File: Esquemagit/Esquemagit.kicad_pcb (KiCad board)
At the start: 2 copper layers, 25 parts, among them U1 LM358, U5 ESP32-WROOM-32

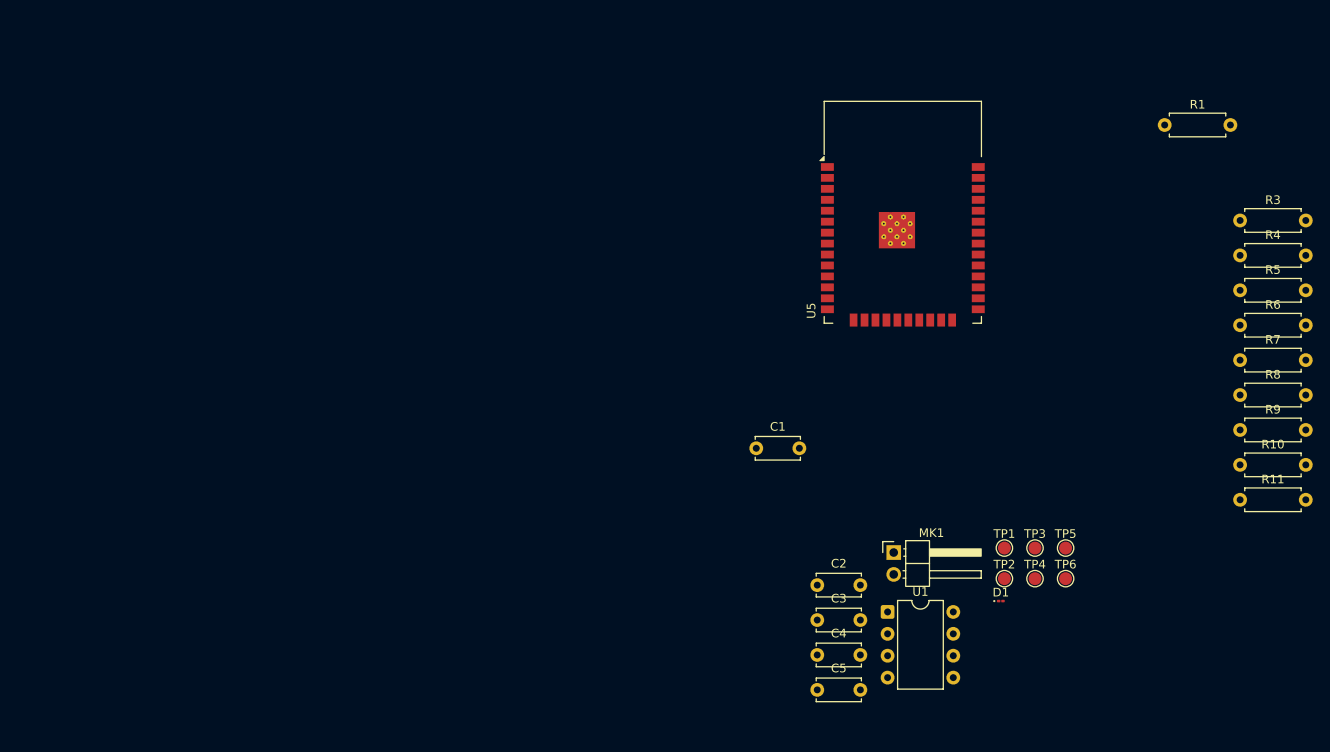
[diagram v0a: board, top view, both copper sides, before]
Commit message: Se agrego huellas, se realizo avances en la etapa de amplificacion en la pcb
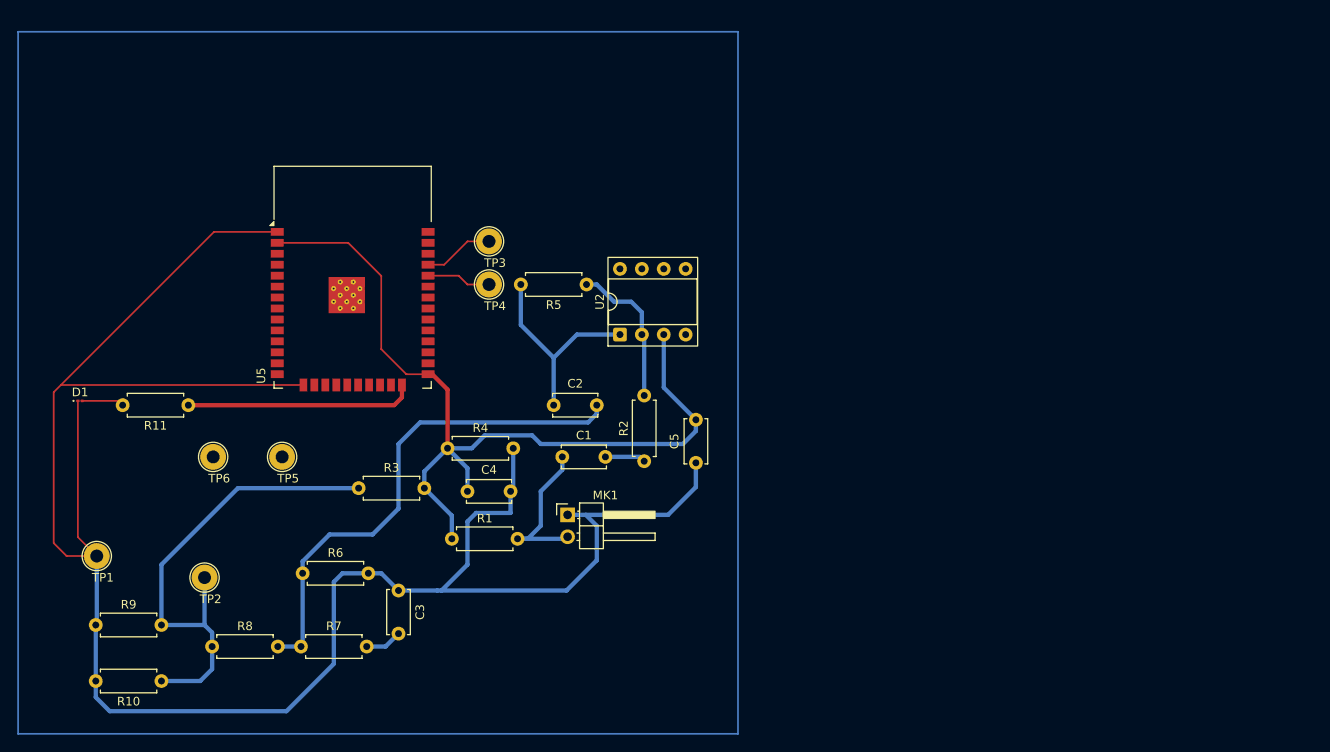
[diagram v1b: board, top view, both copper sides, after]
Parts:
- removed U1: LM358, Package_DIP:DIP-8_W7.62mm
- added R2: 1K, Resistor_THT:R_Axial_DIN0207_L6.3mm_D2.5mm_P7.62mm_Horizontal, F.Cu at (99.5, 103.0)
- added U2: LM358, Package_DIP:DIP-8_W7.62mm_Socket, F.Cu at (96.7, 88.3)
- TP1, TP2, TP3, TP4, TP5, TP6: footprint TestPoint:TestPoint_Pad_D1.5mm -> TestPoint:TestPoint_Loop_D2.54mm_Drill1.5mm_Beaded
- moved R9 134.7 mm to (35.9, 122.0)
- moved R10 127.6 mm to (43.5, 128.5), turned to 180 degrees
- moved R8 122.8 mm to (49.4, 124.5)
- moved R11 122.5 mm to (46.6, 96.5), turned to 180 degrees
- moved R7 113.9 mm to (59.7, 124.5)
- moved R6 112.5 mm to (59.9, 116.0)
- moved D1 109.3 mm to (34.1, 96.0)
- moved R3 106.9 mm to (66.4, 106.1)
- moved TP1 105.3 mm to (36.0, 114.0)
- moved TP6 99.9 mm to (49.5, 102.5)
- moved R1 95.6 mm to (77.2, 112.0)
- moved R4 94.6 mm to (76.7, 101.5)
- moved TP2 92.8 mm to (48.5, 116.5)
- moved TP5 91.5 mm to (57.5, 102.5)
- moved R5 75.8 mm to (92.8, 82.5), turned to 180 degrees
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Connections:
- TP2 pad 1: /+3.3V -> 3.3V
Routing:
- net GND: track 0.00 -> 247.3 mm
- net 3.3V: track 0.00 -> 156.7 mm
- net Net-(C2-Pad2): track 0.00 -> 59.3 mm
- net /LED_CTRL: track 0.00 -> 26.6 mm
- net Net-(C2-Pad1): track 0.00 -> 24.4 mm
- net Net-(MK1-+): track 0.00 -> 18.2 mm
- net Net-(U2A--): track 0.00 -> 17.5 mm
- net /TX: track 0.00 -> 8.19 mm
- net /RX: track 0.00 -> 7.49 mm
- net Net-(D1-A): track 0.00 -> 4.90 mm
- net Net-(C1-Pad2): track 0.00 -> 4.71 mm
- net Net-(C3-Pad2): track 0.00 -> 4.31 mm

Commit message: Realice ajustes de componenetes en pcb y ademas cableado de pistas
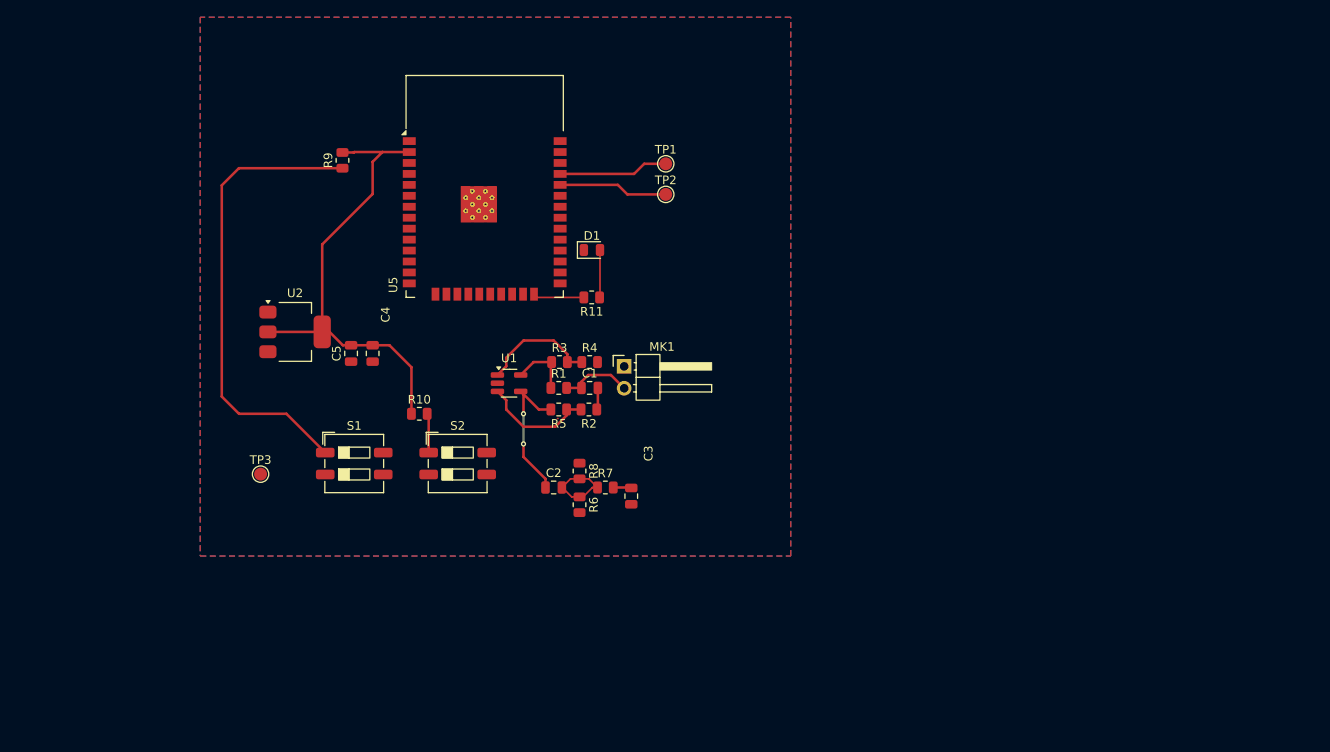
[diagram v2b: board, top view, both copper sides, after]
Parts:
- removed TP4, TP5, TP6: TestPoint, TestPoint:TestPoint_Loop_D2.54mm_Drill1.5mm_Beaded
- added S1: PulsadorMTR_LFS, Button_Switch_SMD:SW_DIP_SPSTx02_Slide_6.7x6.64mm_W6.73mm_P2.54mm_LowProfile_JPin, F.Cu at (65.9, 103.3)
- added S2: PulsadorMTR_LFS, Button_Switch_SMD:SW_DIP_SPSTx02_Slide_6.7x6.64mm_W6.73mm_P2.54mm_LowProfile_JPin, F.Cu at (77.9, 103.3)
- added U1: LMV321, Package_TO_SOT_SMD:SOT-23-5_HandSoldering, F.Cu at (83.8, 94.0)
- C1, C2, C3, C4, C5: footprint Capacitor_THT:C_Disc_D5.0mm_W2.5mm_P5.00mm -> Capacitor_SMD:C_0805_2012Metric
- D1: footprint LED_SMD:LED_01005_0402Metric -> LED_SMD:LED_0805_2012Metric
- R1, R11, R2, R3, R4, R5, R6, R7, R8, R9: footprint Resistor_THT:R_Axial_DIN0207_L6.3mm_D2.5mm_P7.62mm_Horizontal -> Resistor_SMD:R_0805_2012Metric
- R10: value R -> 10; footprint Resistor_THT:R_Axial_DIN0207_L6.3mm_D2.5mm_P7.62mm_Horizontal -> Resistor_SMD:R_0805_2012Metric
- TP1, TP2, TP3: footprint TestPoint:TestPoint_Loop_D2.54mm_Drill1.5mm_Beaded -> TestPoint:TestPoint_Pad_D1.5mm
- U2: value LM358 -> AMS1117-3.3; footprint Package_DIP:DIP-8_W7.62mm_Socket -> Package_TO_SOT_SMD:SOT-223-3_TabPin2
- moved TP1 80.2 mm to (102.0, 68.5)
- moved TP2 69.6 mm to (102.0, 72.0)
- moved D1 61.9 mm to (93.4, 78.5)
- moved R9 61.0 mm to (64.5, 68.1), turned to 90 degrees
- moved R11 48.4 mm to (93.4, 84.0)
- moved R8 47.2 mm to (92.0, 104.1), turned to -90 degrees
- moved R10 43.1 mm to (73.4, 97.5), turned to 0 degrees
- moved C5 42.0 mm to (65.5, 90.5)
- moved R7 39.8 mm to (95.0, 106.0)
- moved TP3 37.8 mm to (55.0, 104.5)
- moved U2 37.7 mm to (59.0, 88.0), turned to 0 degrees
- moved R6 33.1 mm to (92.0, 108.0), turned to -90 degrees
- moved C3 29.1 mm to (98.0, 107.0), turned to 90 degrees
- moved R3 27.5 mm to (89.7, 91.5)
- moved R1 21.4 mm to (89.6, 94.5)
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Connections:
- C2 pad 1: Net-(C2-Pad1) -> /salida
- R10 pad 2: GND -> Net-(S2-COM)
- R11 pad 1: /LED_CTRL -> Net-(D1-A)
- R11 pad 2: Net-(D1-A) -> /LED_CTRL
- R2 pad 2: Net-(U2A--) -> Net-(U1--)
- R3 pad 2: 3.3V -> Net-(U1-+)
- R4 pad 1: 3.3V -> Net-(U1-+)
- R5 pad 1: Net-(U2A--) -> Net-(U1--)
- R5 pad 2: Net-(C2-Pad1) -> /salida
- R9 pad 1: GND -> Net-(S1-COM)
- TP1 pad 1: GND -> /TX
- TP2 pad 1: 3.3V -> /RX
- TP3 pad 1: /TX -> GND
- U2 pad 1: Net-(C2-Pad1) -> Net-(J2-GND_1)
- U2 pad 2: Net-(U2A--) -> 3.3V
- U2 pad 3: 3.3V -> Net-(J2-VBUS_1)
- U5 pad 25: 3.3V -> Net-(S2-COM)
- U5 pad 3: GND -> Net-(S1-COM)
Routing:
- net GND: track 247.3 -> 0.00 mm
- net 3.3V: track 156.7 -> 62.5 mm
- net Net-(S1-COM): track 0.00 -> 54.0 mm
- net Net-(C2-Pad2): track 59.3 -> 10.0 mm
- net Net-(C2-Pad1): track 24.4 -> 0.00 mm
- net /LED_CTRL: track 26.6 -> 5.94 mm
- net Net-(U2A--): track 17.5 -> 0.00 mm
- net /salida: track 0.00 -> 16.7 mm, vias 0 -> 2
- net Net-(U1-+): track 0.00 -> 13.6 mm
- net Net-(U1--): track 0.00 -> 13.3 mm
- net Net-(MK1-+): track 18.2 -> 8.36 mm
- net /RX: track 7.49 -> 12.7 mm
- net Net-(S2-COM): track 0.00 -> 4.57 mm
- net /TX: track 8.19 -> 12.7 mm
- net Net-(C3-Pad2): track 4.31 -> 2.11 mm
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- added copper zone on B.Cu, net GND
- added copper zone on F.Cu, net GND

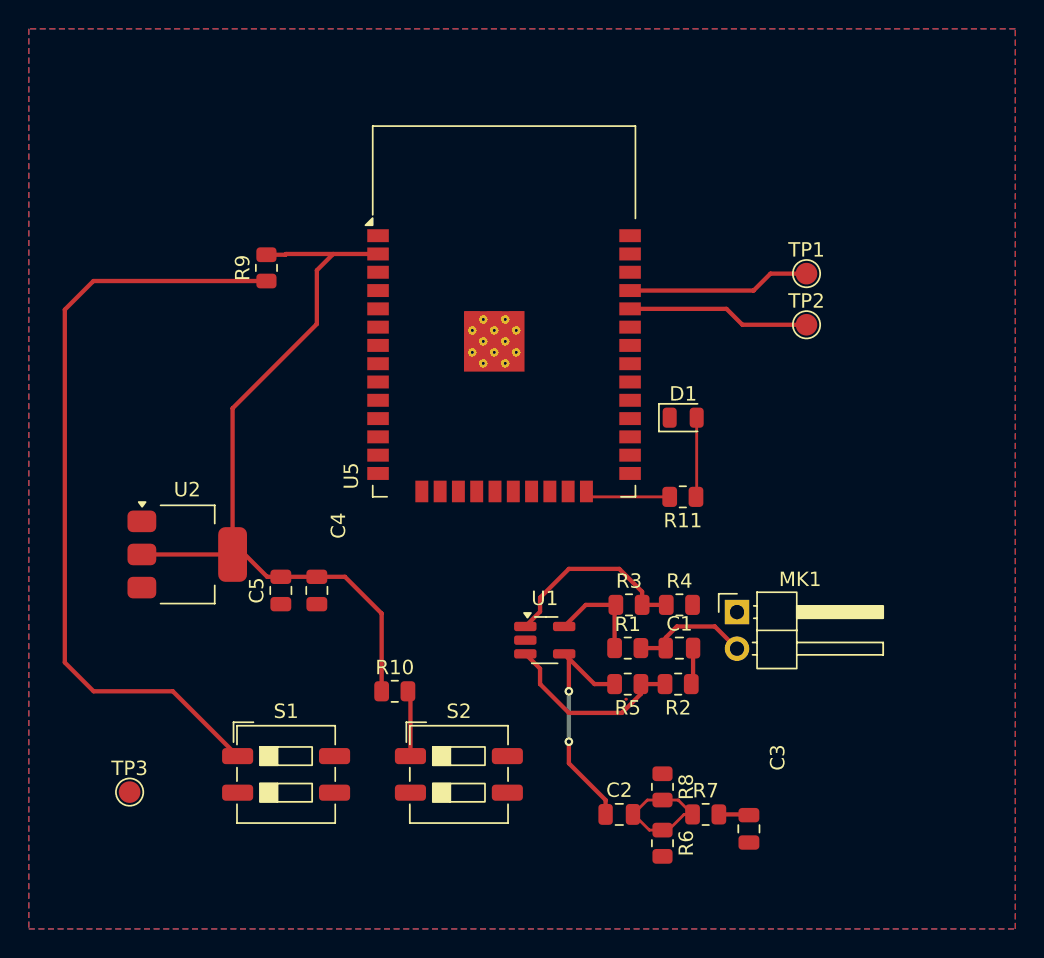
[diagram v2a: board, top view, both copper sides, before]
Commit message: agregue planos de tierra y reorganice componentes
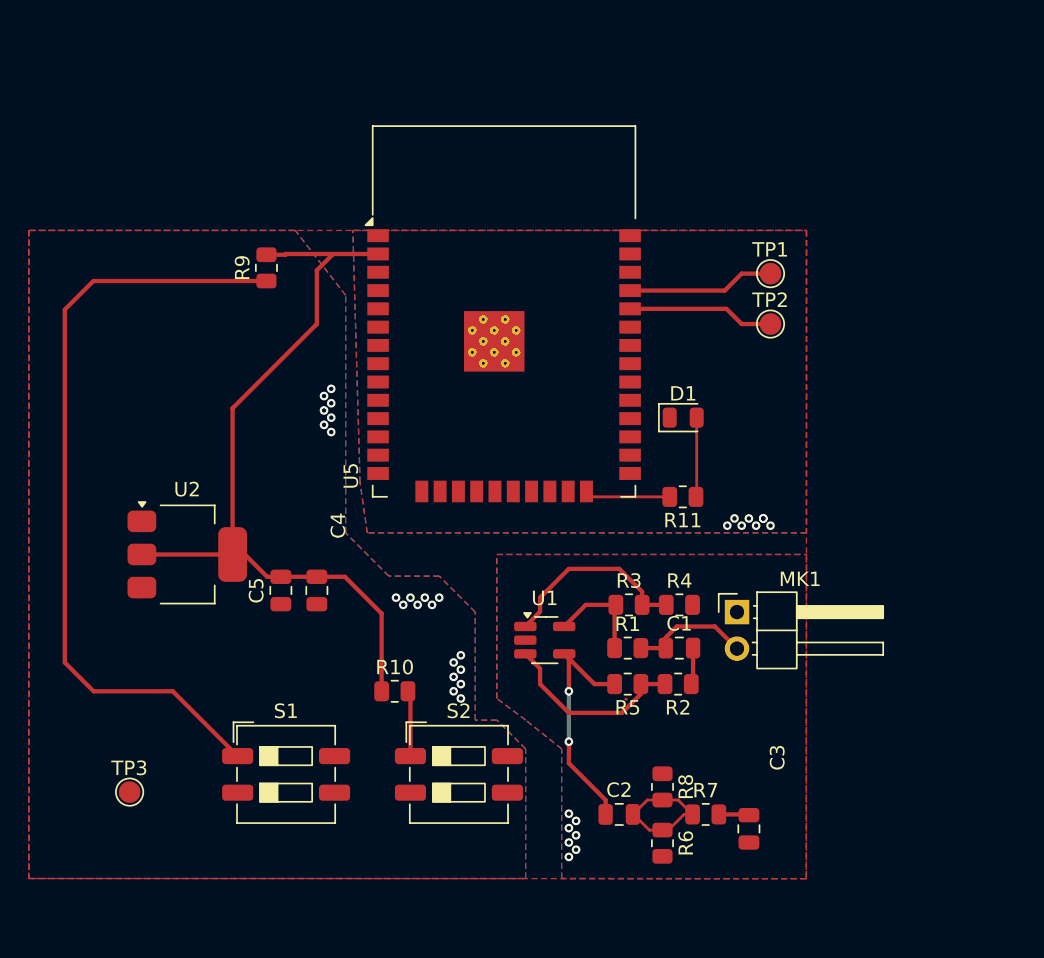
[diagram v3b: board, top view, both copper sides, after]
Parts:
- moved TP2 2.50 mm to (99.5, 72.0)
- moved TP1 2.50 mm to (99.5, 68.5)
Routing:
- net /RX: track 12.7 -> 10.2 mm
- net /TX: track 12.7 -> 10.2 mm
- net GND: vias 0 -> 36

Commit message: Se realizo la adicion de 5 rutas faltantes
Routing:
- net Net-(S2-COM): track 4.57 -> 37.3 mm
- net 3.3V: track 62.5 -> 93.0 mm, vias 0 -> 8
- net Net-(S1-COM): track 54.0 -> 62.0 mm, vias 0 -> 3

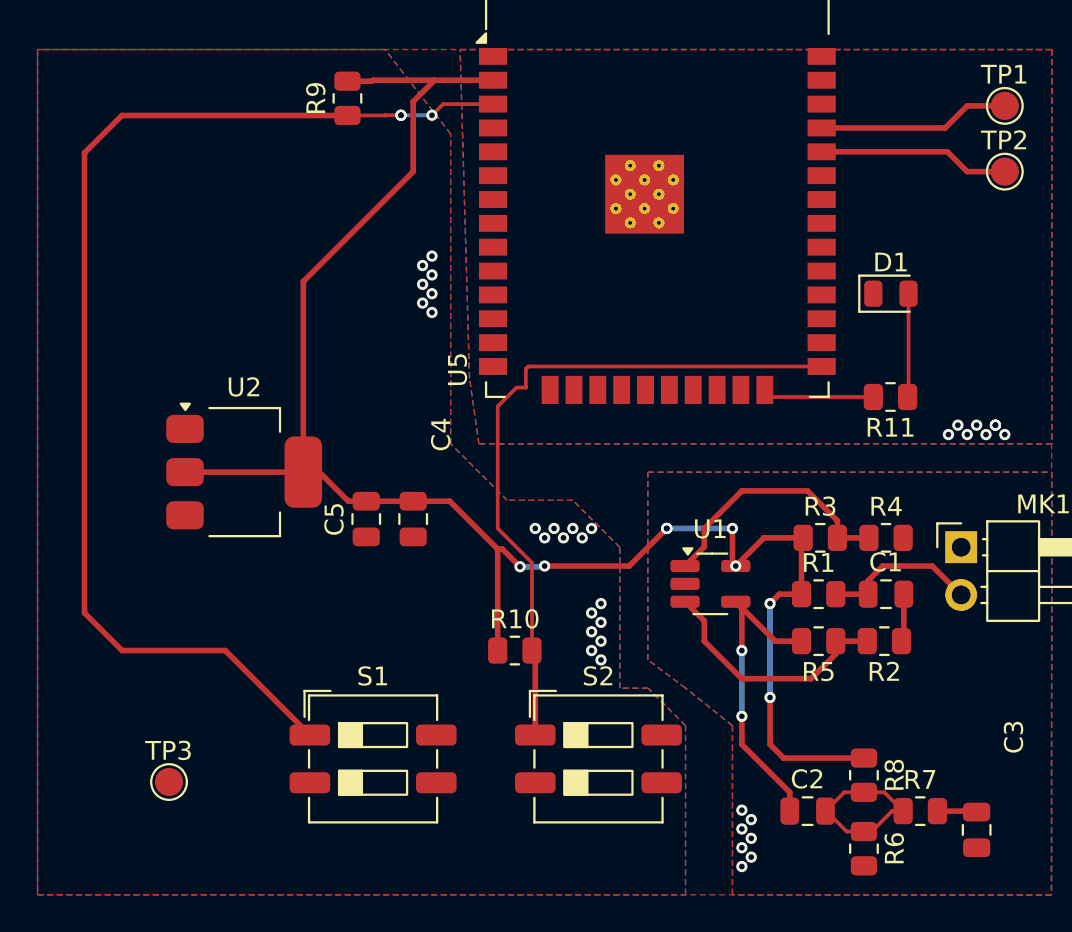
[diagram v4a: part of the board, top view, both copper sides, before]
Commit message: feat:nuevas rutas
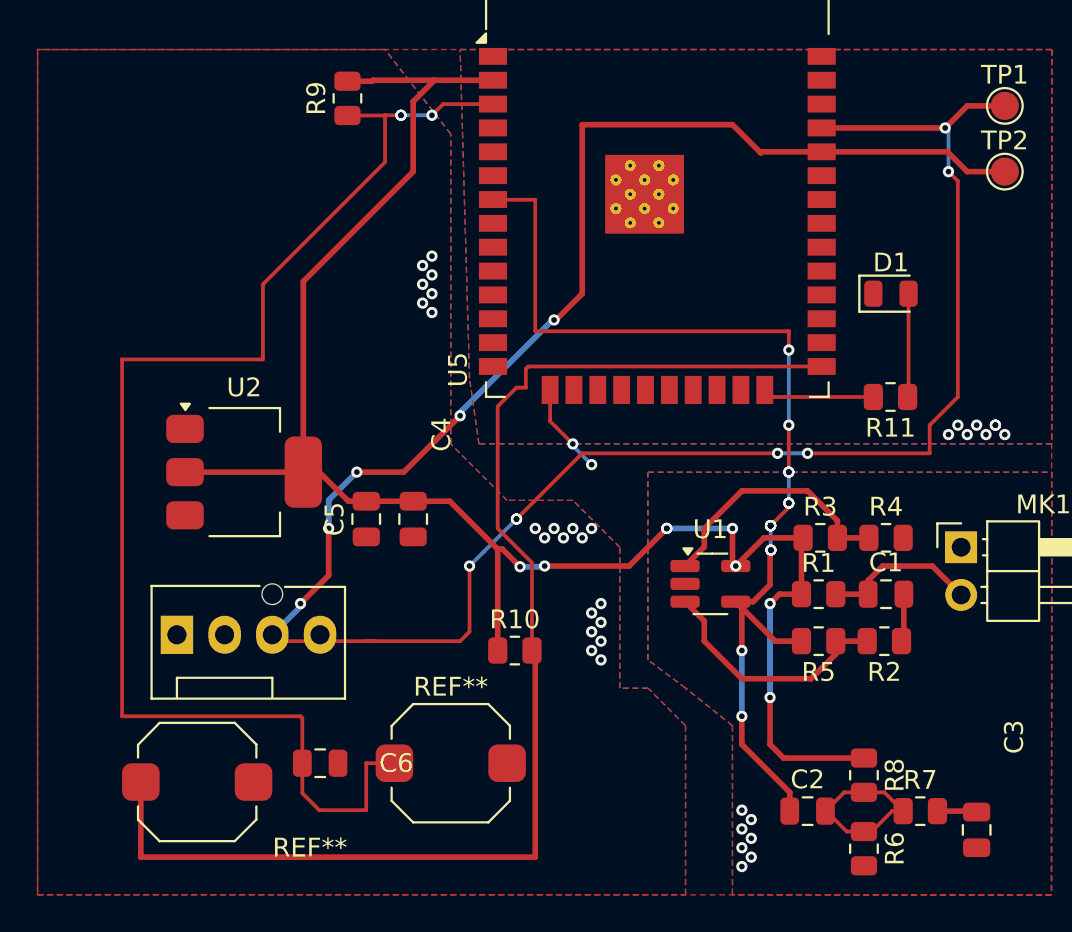
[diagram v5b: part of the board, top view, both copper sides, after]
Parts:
- removed S1, S2: PulsadorMTR_LFS, Button_Switch_SMD:SW_DIP_SPSTx02_Slide_6.7x6.64mm_W6.73mm_P2.54mm_LowProfile_JPin
- removed TP3: TestPoint, TestPoint:TestPoint_Pad_D1.5mm
- added C6: 100nf, Capacitor_SMD:C_0805_2012Metric, F.Cu at (63.0, 103.5)
- added J1: Conn_01x04_Pin, Connector:FanPinHeader_1x04_P2.54mm_Vertical, F.Cu at (55.4, 96.7)
- added SW1: SW_Push, Button_Switch_SMD:SW_Push_1TS009xxxx-xxxx-xxxx_6x6x5mm, F.Cu at (70.0, 103.5)
- added SW2: SW_Push, Button_Switch_SMD:SW_Push_1TS009xxxx-xxxx-xxxx_6x6x5mm, F.Cu at (56.5, 104.5)
- R11: value 150 -> 47 ohm
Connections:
- C2 pad 1: /salida -> salida
- R2 pad 2: Net-(U1--) -> Net-(U1-+)
- R5 pad 2: /salida -> salida
- U1 pad 2: unconnected-(U1-V--Pad2) -> GND
- U1 pad 4: /salida -> salida
- U2 pad 1: Net-(J2-GND_1) -> GND
- U5 pad 14: unconnected-(U5-IO12-Pad14) -> /sck
- U5 pad 21: unconnected-(U5-SDO/SD0-Pad21) -> /g21
- U5 pad 22: unconnected-(U5-SDI/SD1-Pad22) -> /w5
- U5 pad 7: unconnected-(U5-IO35-Pad7) -> salida
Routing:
- net /TX: track 10.2 -> 70.6 mm, vias 0 -> 7
- net salida: track 0.00 -> 55.9 mm, vias 0 -> 14
- net /RX: track 10.2 -> 59.3 mm, vias 0 -> 5
- net Net-(U5-IO0): track 37.3 -> 68.8 mm
- net /salida: track 16.9 -> 0.00 mm, vias 2 -> 0
- net Net-(U5-EN): track 62.0 -> 71.6 mm
- net GND: track 0.00 -> 4.89 mm, vias 36 -> 38
